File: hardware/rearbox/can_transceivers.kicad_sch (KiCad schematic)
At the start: 0 parts

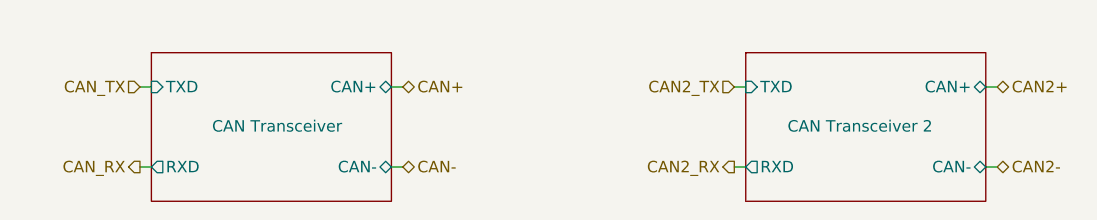
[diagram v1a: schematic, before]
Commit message: Deleted measurement systems for new iteration
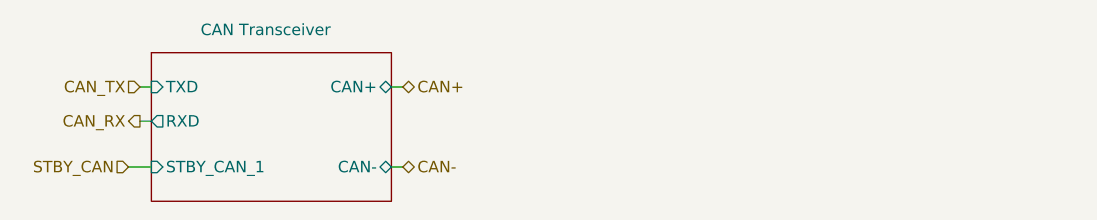
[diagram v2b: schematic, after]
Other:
- removed sheet CAN Transceiver 2
- sheet CAN Transceiver ports: added STBY_CAN_1; removed none
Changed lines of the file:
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@@
 	(wire
 		(pts
-			(xy 101.6 101.6) (xy 102.87 101.6)
+			(xy 101.6 96.52) (xy 102.87 96.52)
 		)
 		(stroke
@@
 	(wire
 		(pts
-			(xy 167.64 92.71) (xy 168.91 92.71)
+			(xy 100.33 101.6) (xy 102.87 101.6)
 		)
 		(stroke
@@
 	(wire
 		(pts
-			(xy 167.64 101.6) (xy 168.91 101.6)
-		)
-		(stroke
-			(width 0)
-			(type default)
-		)
-	)
-	(wire
-		(pts
 			(xy 101.6 92.71) (xy 102.87 92.71)
 		)
@@
 		)
 	)
-	(wire
-		(pts
-			(xy 195.58 92.71) (xy 196.85 92.71)
-		)
-		(stroke
-			(width 0)
-			(type default)
-		)
-	)
-	(wire
-		(pts
-			(xy 195.58 101.6) (xy 196.85 101.6)
-		)
-		(stroke
-			(width 0)
-			(type default)
-		)
-	)
-	(hierarchical_label "CAN2_RX"
-		(shape output)
-		(at 167.64 101.6 180)
+	(hierarchical_label "STBY_CAN"
+		(shape input)
+		(at 100.33 101.6 180)
 		(effects
 			(font
@@
 			)
 			(justify right)
-		)
-	)
-	(hierarchical_label "CAN2+"
-		(shape bidirectional)
-		(at 196.85 92.71 0)
-		(effects
-			(font
-				(size 1.27 1.27)
-			)
-			(justify left)
 		)
 	)
@@
 		)
 	)
-	(hierarchical_label "CAN2-"
-		(shape bidirectional)
-		(at 196.85 101.6 0)
-		(effects
-			(font
-				(size 1.27 1.27)
-			)
-			(justify left)
-		)
-	)
 	(hierarchical_label "CAN_RX"
 		(shape output)
-		(at 101.6 101.6 180)
-		(effects
-			(font
-				(size 1.27 1.27)
-			)
-			(justify right)
-		)
-	)
-	(hierarchical_label "CAN2_TX"
-		(shape input)
-		(at 167.64 92.71 180)
+		(at 101.6 96.52 180)
 		(effects
 			(font
@@
 		)
 		(property "Sheetname" "CAN Transceiver"
-			(at 116.84 97.0784 0)
+			(at 115.57 86.36 0)
 			(effects
 				(font
@@
 		)
 		(pin "RXD" output
-			(at 102.87 101.6 180)
+			(at 102.87 96.52 180)
 			(effects
 				(font
@@
 			)
 		)
+		(pin "STBY_CAN_1" input
+			(at 102.87 101.6 180)
+			(effects
+				(font
+					(size 1.27 1.27)
+				)
+				(justify left)
+			)
+		)
 		(instances
 			(project "suspension_tension_meter"
@@
 				)
 			)
-		)
-	)
-	(sheet
-		(at 168.91 88.9)
-		(size 26.67 16.51)
-		(exclude_from_sim no)
-		(in_bom yes)
-		(on_board yes)
-		(dnp no)
-		(stroke
-			(width 0.1524)
-			(type solid)
-		)
-		(fill
-			(color 0 0 0 0.0000)
-		)
-		(property "Sheetname" "CAN Transceiver 2"
-			(at 181.61 97.0784 0)
-			(effects
-				(font
-					(size 1.27 1.27)
-				)
-			)
-		)
-		(property "Sheetfile" "can_transceiver.kicad_sch"
-			(at 168.91 105.9946 0)
-			(effects
-				(font
-					(size 1.27 1.27)
-				)
-				(justify left top)
-				(hide yes)
-			)
-		)
-		(pin "RXD" output
-			(at 168.91 101.6 180)
-			(effects
-				(font
-					(size 1.27 1.27)
-				)
-				(justify left)
-			)
-		)
-		(pin "TXD" input
-			(at 168.91 92.71 180)
-			(effects
-				(font
-					(size 1.27 1.27)
-				)
-				(justify left)
-			)
-		)
-		(pin "CAN-" bidirectional
-			(at 195.58 101.6 0)
-			(effects
-				(font
-					(size 1.27 1.27)
-				)
-				(justify right)
-			)
-		)
-		(pin "CAN+" bidirectional
-			(at 195.58 92.71 0)
-			(effects
-				(font
-					(size 1.27 1.27)
-				)
-				(justify right)
-			)
-		)
-		(instances
-			(project "suspension_tension_meter"
-				(path "/d29c2854-1cff-48df-9335-a3932490d817"
-					(page "4")
-				)
-			)
-			(project "rearbox"
-				(path "/b652b05a-4e3d-4ad1-b032-18886abe7d45/38408e41-dfb1-4c27-acb0-3f1224cc8789"
-					(page "6")
-				)
-			)
